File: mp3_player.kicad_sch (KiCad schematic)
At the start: 36 parts, among them J1 USB_B_Micro, J2 Micro_SD_Card, SW1 SW_SPST, SW2 SW_Push, SW3 SW_Push, SW4 SW_Push, SW5 SW_Push_SPDT, U1 VS1053B, U2 TP4056, U3 MT3608, U7 DW01A, U8 FS8205A

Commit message: Hierarchical design for submodules
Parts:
- removed BT1: Battery, symbol Device:Battery
- removed C1, C2: 22uF, symbol Device:C
- removed C3, C6: 10uF, symbol Device:C
- removed C4, C5: 0,1uF, symbol Device:C
- removed D1: SS34, Diode_SMD:D_SMA, symbol Diode:SS34
- removed D2, D3: LED, symbol Device:LED
- removed J1: USB_B_Micro, symbol Connector:USB_B_Micro
- removed J2: Micro_SD_Card, symbol Connector:Micro_SD_Card
- removed L1: 22uH, symbol Device:L
- removed R1: 2.2kΩ, symbol Device:R
- removed R10, R7, R8, R9: 10kΩ, symbol Device:R
- removed R2, R3, R6: 1kΩ, symbol Device:R
- removed R4: 1,2kΩ, symbol Device:R
- removed R5: 100Ω, symbol Device:R
- removed RV1: R_Potentiometer, symbol Device:R_Potentiometer
- removed U2: TP4056, MyKl_Footprints:TP4056_Footpring, symbol Battery_Management:TP4056
- removed U3: MT3608, Package_TO_SOT_SMD:SOT-23-6, symbol Regulator_Switching:MT3608
- removed U7: DW01A, Package_TO_SOT_SMD:SOT-23-6, symbol Battery_Management:DW01A
- removed U8: FS8205A, MyKl_Footprints:8205A_Footprint, symbol MyKl_Symbols:FS8205A
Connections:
- no-connect marks 8 -> 0
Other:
- added sheet MT360B Step Up Boost Converter (step_up_boost_converter.kicad_sch)
- added sheet MicroSD Card Reader to SPI (microSD_SPI_adapter.kicad_sch)
- added sheet TP4056 LIPO Charger with Protection (lipo_bat_charger.kicad_sch)
- note removed: "MT3608 2V-28V Micro-USB Step Up Boost Power Supply Voltage Converter Module"
- note removed: "MicroSD Card Reader to SPI Adapter"
- note removed: "TP4056 Lithium Battery Charger and Protection Module"

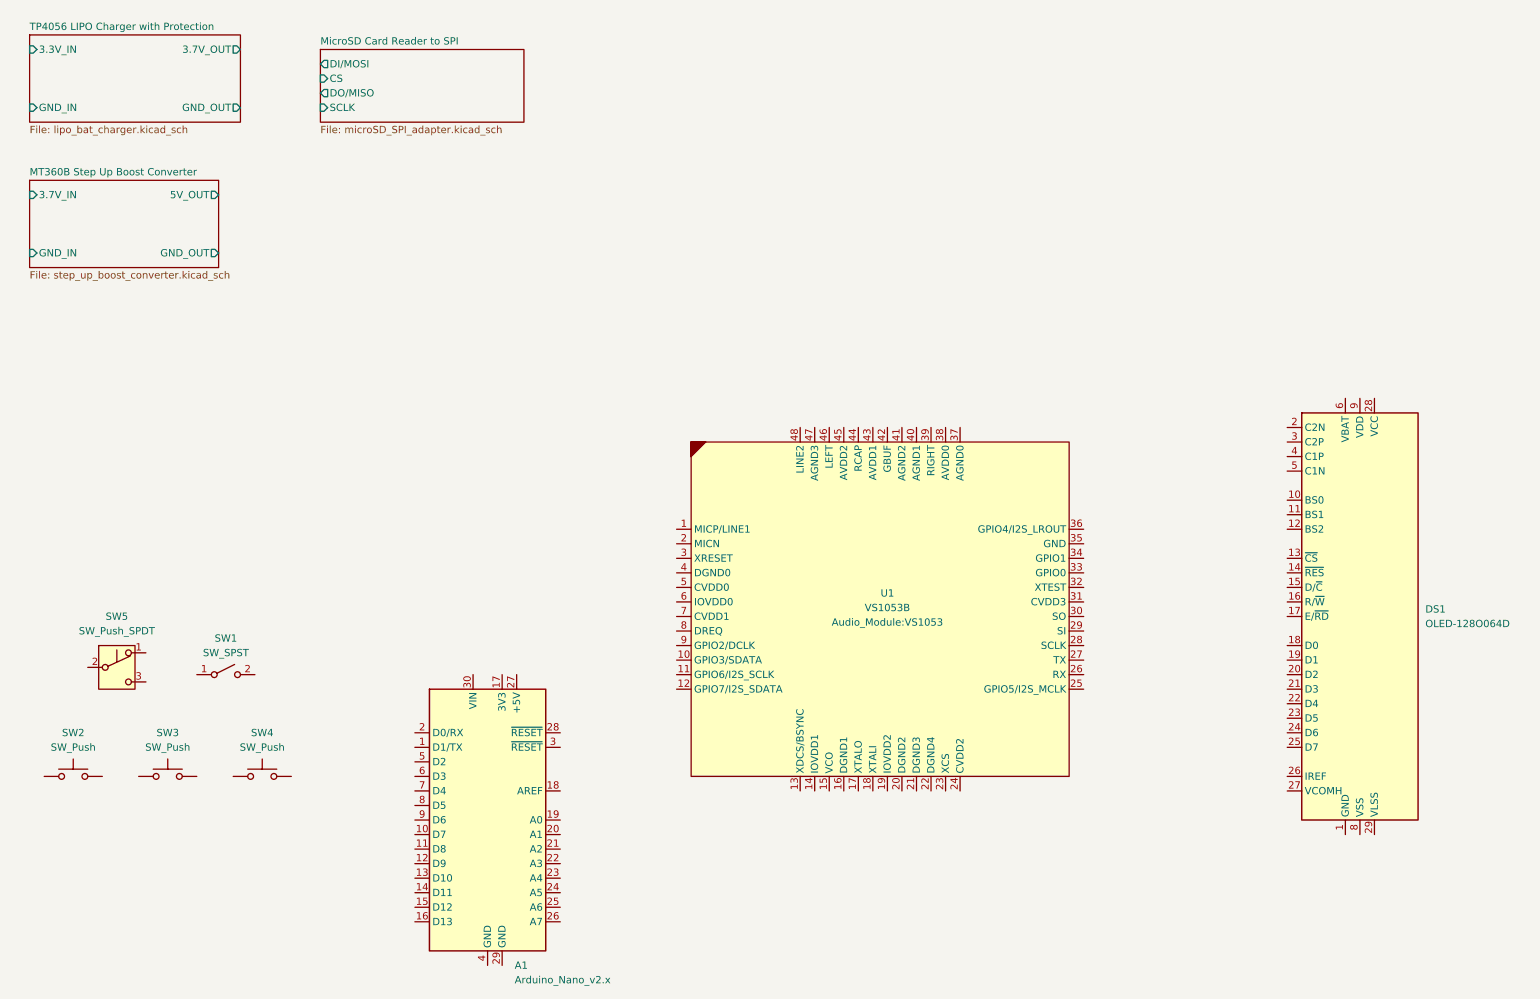
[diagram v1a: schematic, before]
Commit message: Added OLED Display Module
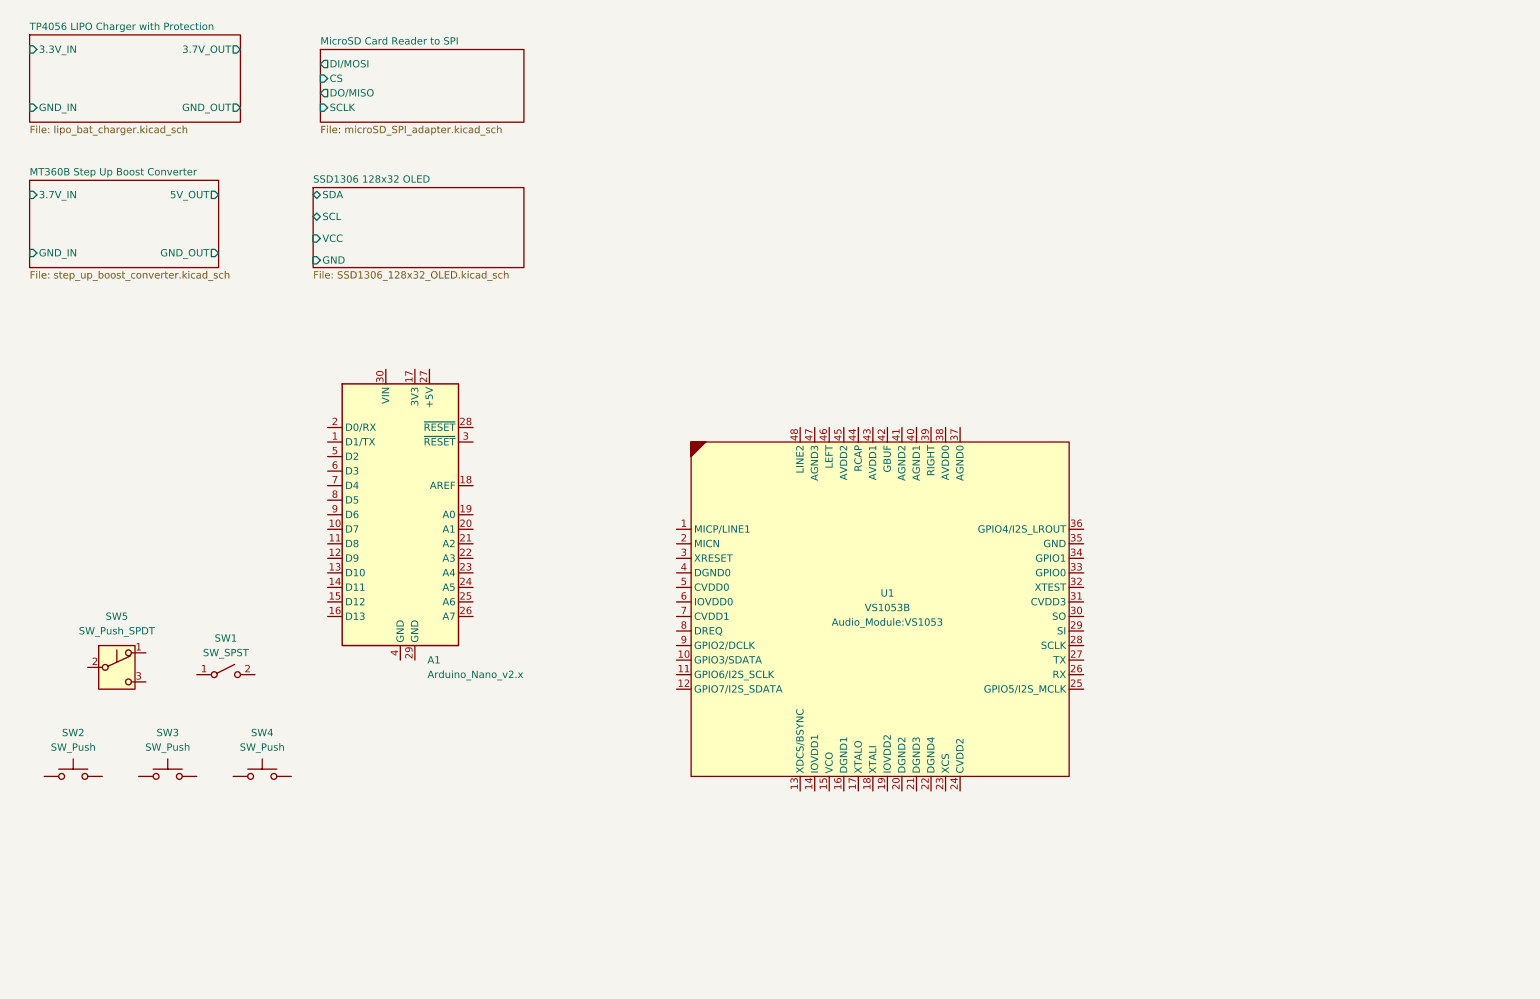
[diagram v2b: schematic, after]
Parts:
- removed DS1: OLED-128O064D, Display:OLED-128O064D, symbol Display_Graphic:OLED-128O064D
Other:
- added sheet SSD1306 128x32 OLED (SSD1306_128x32_OLED.kicad_sch)
- moved on the sheet: A1
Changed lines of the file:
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@@
-	)
-	(symbol
-		(lib_id "Display_Graphic:OLED-128O064D")
-		(at 247.65 119.38 0)
-		(unit 1)
-		(exclude_from_sim no)
-		(in_bom yes)
-		(on_board yes)
-		(dnp no)
-		(fields_autoplaced yes)
-		(property "Reference" "DS1"
-			(at 259.08 118.1099 0)
-			(effects
-				(font
-					(size 1.27 1.27)
-				)
-				(justify left)
-			)
-		)
-		(property "Value" "OLED-128O064D"
-			(at 259.08 120.6499 0)
-			(effects
-				(font
-					(size 1.27 1.27)
-				)
-				(justify left)
-			)
-		)
-		(property "Footprint" "Display:OLED-128O064D"
-			(at 247.65 119.38 0)
-			(effects
-				(font
-					(size 1.27 1.27)
-				)
-				(hide yes)
-			)
-		)
-		(property "Datasheet" "https://www.vishay.com/docs/37902/oled128o064dbpp3n00000.pdf"
-			(at 247.65 99.06 0)
-			(effects
-				(font
-					(size 1.27 1.27)
-				)
-				(hide yes)
-			)
-		)
-		(property "Description" "OLED display 128x64"
-			(at 247.65 119.38 0)
-			(effects
-				(font
-					(size 1.27 1.27)
-				)
-				(hide yes)
-			)
-		)
-		(pin "30"
-		)
-		(pin "20"
-		)
-		(pin "16"
-		)
-		(pin "10"
-		)
-		(pin "11"
-		)
-		(pin "21"
-		)
-		(pin "3"
-		)
-		(pin "17"
-		)
-		(pin "14"
-		)
-		(pin "13"
-		)
-		(pin "1"
-		)
-		(pin "8"
-		)
-		(pin "18"
-		)
-		(pin "19"
-		)
-		(pin "9"
-		)
-		(pin "22"
-		)
-		(pin "15"
-		)
-		(pin "5"
-		)
-		(pin "4"
-		)
-		(pin "2"
-		)
-		(pin "7"
-		)
-		(pin "12"
-		)
-		(pin "29"
-		)
-		(pin "28"
-		)
-		(pin "23"
-		)
-		(pin "27"
-		)
-		(pin "26"
-		)
-		(pin "25"
-		)
-		(pin "24"
-		)
-		(pin "6"
-		)
-		(instances
-			(project ""
-				(path "/2c361aad-9218-45b1-882d-1b23ed962d51"
-					(reference "DS1")
-					(unit 1)
-				)
-			)
-		)
 	)
 	(symbol
@@
 	(symbol
 		(lib_id "MCU_Module:Arduino_Nano_v2.x")
-		(at 95.25 154.94 0)
+		(at 80.01 101.6 0)
 		(unit 1)
 		(exclude_from_sim no)
@@
 		(fields_autoplaced yes)
 		(property "Reference" "A1"
-			(at 99.9841 180.34 0)
+			(at 84.7441 127 0)
 			(effects
 				(font
@@
 		)
 		(property "Value" "Arduino_Nano_v2.x"
-			(at 99.9841 182.88 0)
+			(at 84.7441 129.54 0)
 			(effects
 				(font
@@
 		)
 		(property "Footprint" "Module:Arduino_Nano"
-			(at 95.25 154.94 0)
+			(at 80.01 101.6 0)
 			(effects
 				(font
@@
 		)
 		(property "Datasheet" "https://www.arduino.cc/en/uploads/Main/ArduinoNanoManual23.pdf"
-			(at 95.25 154.94 0)
+			(at 80.01 101.6 0)
 			(effects
 				(font
@@
 		)
 		(property "Description" "Arduino Nano v2.x"
-			(at 95.25 154.94 0)
+			(at 80.01 101.6 0)
 			(effects
 				(font
@@
 				)
 			)
+		)
+	)
+	(sheet
+		(at 64.77 44.45)
+		(size 36.83 13.97)
+		(exclude_from_sim no)
+		(in_bom yes)
+		(on_board yes)
+		(dnp no)
+		(fields_autoplaced yes)
+		(stroke
+			(width 0.1524)
+			(type solid)
+		)
+		(fill
+			(color 0 0 0 0.0000)
+		)
+		(property "Sheetname" "SSD1306 128x32 OLED"
+			(at 64.77 43.7384 0)
+			(effects
+				(font
+					(size 1.27 1.27)
+				)
+				(justify left bottom)
+			)
+		)
+		(property "Sheetfile" "SSD1306_128x32_OLED.kicad_sch"
+			(at 64.77 59.0046 0)
+			(effects
+				(font
+					(size 1.27 1.27)
+				)
+				(justify left top)
+			)
+		)
+		(pin "GND" input
+			(at 64.77 57.15 180)
+			(effects
+				(font
+					(size 1.27 1.27)
+				)
+				(justify left)
+			)
+		)
+		(pin "SCL" bidirectional
+			(at 64.77 49.53 180)
+			(effects
+				(font
+					(size 1.27 1.27)
+				)
+				(justify left)
+			)
+		)
+		(pin "SDA" bidirectional
+			(at 64.77 45.72 180)
+			(effects
+				(font
+					(size 1.27 1.27)
+				)
+				(justify left)
+			)
+		)
+		(pin "VCC" input
+			(at 64.77 53.34 180)
+			(effects
+				(font
+					(size 1.27 1.27)
+				)
+				(justify left)
+			)
+		)
+		(instances
+			(project "mp3_player"
+				(path "/2c361aad-9218-45b1-882d-1b23ed962d51"
+					(page "5")
+				)
+			)

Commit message: Code, drivers patch, and pcb updates
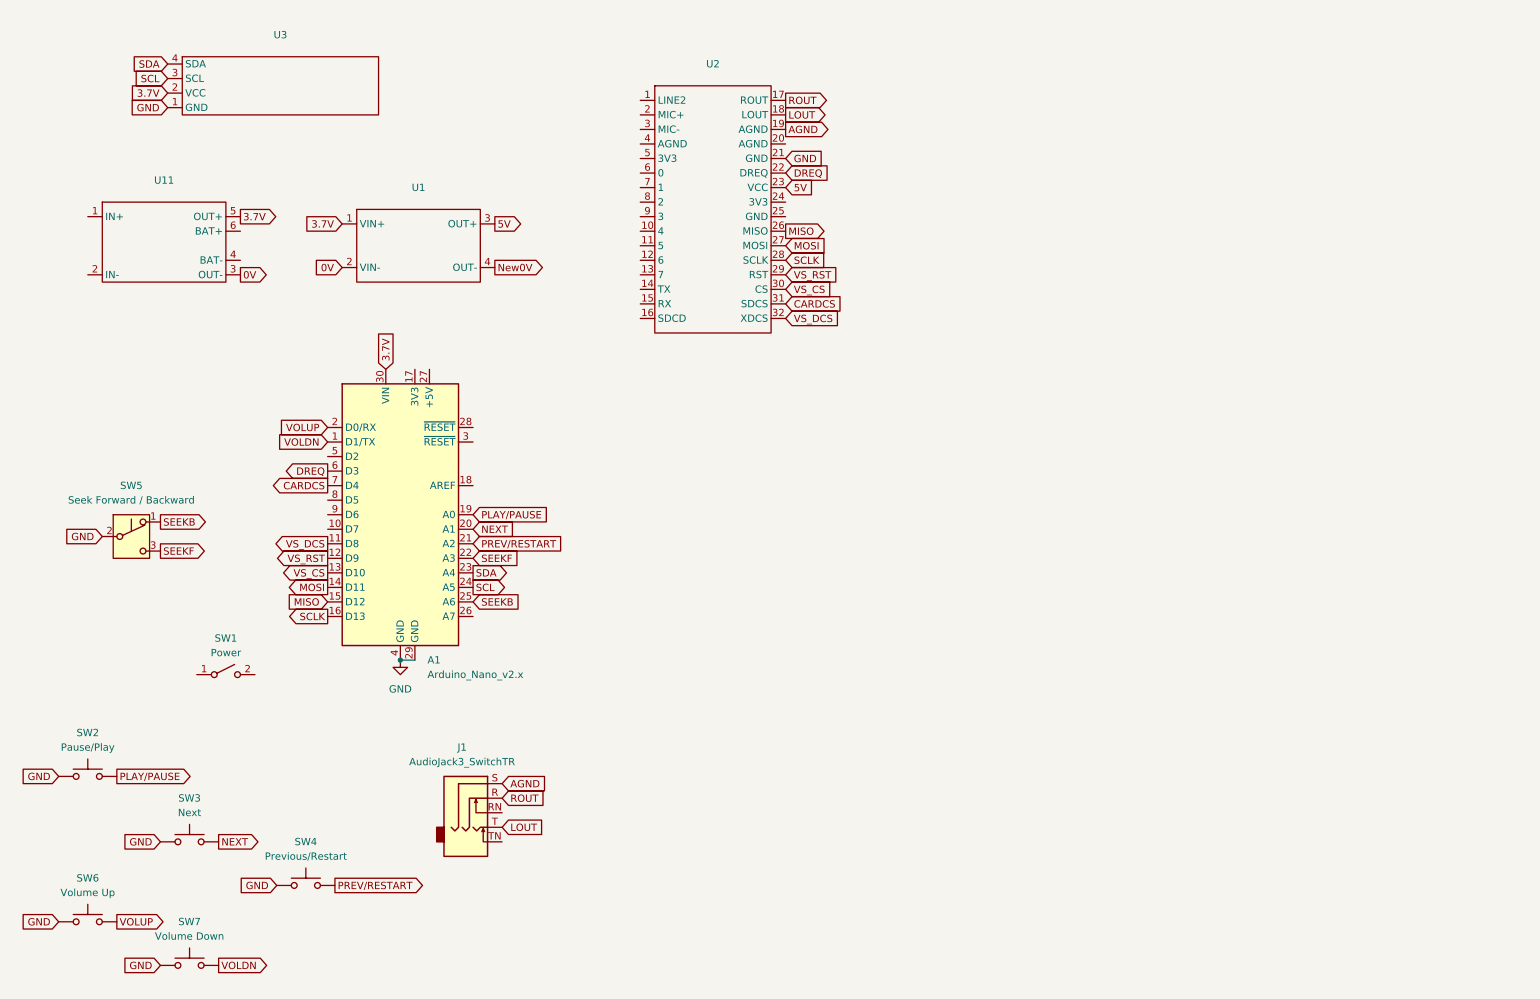
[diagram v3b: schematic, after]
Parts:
- removed U1: VS1053B, Audio_Module:VS1053, symbol Audio:VS1053B
- added J1: AudioJack3_SwitchTR, Connector_Audio:Jack_3.5mm_CUI_SJ1-3525N_Horizontal, symbol Connector_Audio:AudioJack3_SwitchTR
- added SW6: Volume Up, Button_Switch_THT:SW_PUSH_6mm, symbol Switch:SW_Push
- added SW7: Volume Down, Button_Switch_THT:SW_PUSH_6mm, symbol Switch:SW_Push
- added U1: ~, Converter_DCDC:MT3608_Step_Up_Boost_Converter, symbol Regulator_Switching:Mt3608 2V-28V Step Up Boost Converter
- added U11: ~, Battery:TP4056_LIPO_Charger_Protection_Module, symbol Battery_Management:TP4056_LIPO_Battery_Charger_and_Protection_Module
- added U2: ~, Module:Adafruit_VS1053_Breakout_Board, symbol MCU_Module:Adafruit_VS1053_Breakout_Board
- added U3: ~, Display:SSD1306-0.91-OLED-4pin-128x32, symbol Display_Graphic:SSD1306_OLED_I2C_Module
- SW1: value SW_SPST -> Power; footprint (none) -> Button_Switch_THT:SW_DIP_SPSTx01_Slide_6.7x4.1mm_W7.62mm_P2.54mm_LowProfile
- SW2: value SW_Push -> Pause/Play; footprint (none) -> Button_Switch_THT:SW_PUSH_6mm
- SW3: value SW_Push -> Next; footprint (none) -> Button_Switch_THT:SW_PUSH_6mm
- SW4: value SW_Push -> Previous/Restart; footprint (none) -> Button_Switch_THT:SW_PUSH_6mm
- SW5: value SW_Push_SPDT -> Seek Forward / Backward; footprint (none) -> Button_Switch_THT:SW_XKB_DM1-16UC-1
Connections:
- net SEEKB: now reaches SW5.1 (A)
- net SEEKB: now also A1.25 (A6)
- net GND: now reaches SW5.2 (B)
- net GND: now also A1.29 (GND), A1.4 (GND), SW2.1, SW3.1, SW4.1, SW6.1, SW7.1, U2.21 (GND), U3.1 (GND)
- net SEEKF: now reaches SW5.3 (C)
- net SEEKF: now also A1.22 (A3)
- net NEXT: now reaches SW3.2
- net NEXT: now also A1.20 (A1)
- net PREV/RESTART: now reaches SW4.2
- net PREV/RESTART: now also A1.21 (A2)
- net PLAY/PAUSE: now reaches SW2.2
- net PLAY/PAUSE: now also A1.19 (A0)
- net VOLDN: now reaches A1.1 (D1/TX)
- net VOLDN: now also SW7.2
- net VS_DCS: now reaches A1.11 (D8)
- net VS_DCS: now also U2.32 (XDCS)
- net VS_RST: now reaches A1.12 (D9)
- net VS_RST: now also U2.29 (RST)
- net VS_CS: now reaches A1.13 (D10)
- net VS_CS: now also U2.30 (CS)
- net MOSI: now reaches A1.14 (D11)
- net MOSI: now also U2.27 (MOSI)
- net MISO: now reaches A1.15 (D12)
- net MISO: now also U2.26 (MISO)
- net SCLK: now reaches A1.16 (D13)
- net SCLK: now also U2.28 (SCLK)
- net VOLUP: now reaches A1.2 (D0/RX)
- net VOLUP: now also SW6.2
- net SDA: now reaches A1.23 (A4)
- net SDA: now also U3.4 (SDA)
- net SCL: now reaches A1.24 (A5)
- net SCL: now also U3.3 (SCL)
- net 3.7V: now reaches A1.30 (VIN)
- net 3.7V: now also U1.1 (VIN+), U11.5 (OUT+), U3.2 (VCC)
- net DREQ: now reaches A1.6 (D3)
- net DREQ: now also U2.22 (DREQ)
- net CARDCS: now reaches A1.7 (D4)
- net CARDCS: now also U2.31 (SDCS)
- new net 0V: U1.2 (VIN-), U11.3 (OUT-)
- new net 5V: U1.3 (OUT+), U2.23 (VCC)
- new net AGND: J1.S, U2.19 (AGND)
- new net LOUT: J1.T, U2.18 (LOUT)
- new net New0V: U1.4 (OUT-)
- new net ROUT: J1.R, U2.17 (ROUT)
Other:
- removed sheet MT360B Step Up Boost Converter
- removed sheet MicroSD Card Reader to SPI
- removed sheet SSD1306 128x32 OLED
- removed sheet TP4056 LIPO Charger with Protection
- moved on the sheet: SW2, SW3, SW4, SW5
